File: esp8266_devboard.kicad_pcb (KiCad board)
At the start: 2 copper layers, 26.7 x 41.3 mm, 28 parts, among them P1 USB_OTG, P2 CONN_01X09, P3 CONN_01X09, SW1 MODE, SW2 RESET, U1 FT230X, U2 XC6206, U3 esp-wroom-02

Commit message: add OSHW symbol
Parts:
- added Symbol1: Symbol_OSHW-Logo_SilkScreen, Symbols:Symbol_OSHW-Logo_SilkScreen, F.Cu at (153.7, 81.7)
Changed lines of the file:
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@@
     (tracks 291)
     (zones 0)
-    (modules 28)
+    (modules 29)
     (nets 35)
   )
@@
     )
   )
+  (module Symbols:Symbol_OSHW-Logo_SilkScreen (layer F.Cu)
+    (at 153.67 81.661)
+    (descr "Symbol, OSHW-Logo, Silk Screen,")
+    (tags "Symbol, OSHW-Logo, Silk Screen,")
+    (fp_text reference Symbol1 (at 0.127 -0.127) (layer F.SilkS) hide
+      (effects (font (size 1 1) (thickness 0.15)))
+    )
+    (fp_text value Symbol_OSHW-Logo_SilkScreen (at 0.30988 6.56082) (layer F.Fab)
+      (effects (font (size 1 1) (thickness 0.15)))
+    )
+    (fp_line (start 1.66878 2.68986) (end 2.02946 4.16052) (layer F.SilkS) (width 0.15))
+    (fp_line (start 2.02946 4.16052) (end 2.30886 3.0988) (layer F.SilkS) (width 0.15))
+    (fp_line (start 2.30886 3.0988) (end 2.61874 4.17068) (layer F.SilkS) (width 0.15))
+    (fp_line (start 2.61874 4.17068) (end 2.9591 2.72034) (layer F.SilkS) (width 0.15))
+    (fp_line (start 0.24892 3.38074) (end 1.03886 3.37058) (layer F.SilkS) (width 0.15))
+    (fp_line (start 1.03886 3.37058) (end 1.04902 3.38074) (layer F.SilkS) (width 0.15))
+    (fp_line (start 1.04902 3.38074) (end 1.04902 3.37058) (layer F.SilkS) (width 0.15))
+    (fp_line (start 1.08966 2.65938) (end 1.08966 4.20116) (layer F.SilkS) (width 0.15))
+    (fp_line (start 0.20066 2.64922) (end 0.20066 4.21894) (layer F.SilkS) (width 0.15))
+    (fp_line (start 0.20066 4.21894) (end 0.21082 4.20878) (layer F.SilkS) (width 0.15))
+    (fp_line (start -0.35052 2.75082) (end -0.70104 2.66954) (layer F.SilkS) (width 0.15))
+    (fp_line (start -0.70104 2.66954) (end -1.02108 2.65938) (layer F.SilkS) (width 0.15))
+    (fp_line (start -1.02108 2.65938) (end -1.25984 2.86004) (layer F.SilkS) (width 0.15))
+    (fp_line (start -1.25984 2.86004) (end -1.29032 3.12928) (layer F.SilkS) (width 0.15))
+    (fp_line (start -1.29032 3.12928) (end -1.04902 3.37058) (layer F.SilkS) (width 0.15))
+    (fp_line (start -1.04902 3.37058) (end -0.6604 3.50012) (layer F.SilkS) (width 0.15))
+    (fp_line (start -0.6604 3.50012) (end -0.48006 3.66014) (layer F.SilkS) (width 0.15))
+    (fp_line (start -0.48006 3.66014) (end -0.43942 3.95986) (layer F.SilkS) (width 0.15))
+    (fp_line (start -0.43942 3.95986) (end -0.67056 4.18084) (layer F.SilkS) (width 0.15))
+    (fp_line (start -0.67056 4.18084) (end -0.9906 4.20878) (layer F.SilkS) (width 0.15))
+    (fp_line (start -0.9906 4.20878) (end -1.34112 4.09956) (layer F.SilkS) (width 0.15))
+    (fp_line (start -2.37998 2.64922) (end -2.6289 2.66954) (layer F.SilkS) (width 0.15))
+    (fp_line (start -2.6289 2.66954) (end -2.8702 2.91084) (layer F.SilkS) (width 0.15))
+    (fp_line (start -2.8702 2.91084) (end -2.9591 3.40106) (layer F.SilkS) (width 0.15))
+    (fp_line (start -2.9591 3.40106) (end -2.93116 3.74904) (layer F.SilkS) (width 0.15))
+    (fp_line (start -2.93116 3.74904) (end -2.7305 4.06908) (layer F.SilkS) (width 0.15))
+    (fp_line (start -2.7305 4.06908) (end -2.47904 4.191) (layer F.SilkS) (width 0.15))
+    (fp_line (start -2.47904 4.191) (end -2.16916 4.11988) (layer F.SilkS) (width 0.15))
+    (fp_line (start -2.16916 4.11988) (end -1.95072 3.93954) (layer F.SilkS) (width 0.15))
+    (fp_line (start -1.95072 3.93954) (end -1.8796 3.4798) (layer F.SilkS) (width 0.15))
+    (fp_line (start -1.8796 3.4798) (end -1.9304 3.07086) (layer F.SilkS) (width 0.15))
+    (fp_line (start -1.9304 3.07086) (end -2.03962 2.78892) (layer F.SilkS) (width 0.15))
+    (fp_line (start -2.03962 2.78892) (end -2.4003 2.65938) (layer F.SilkS) (width 0.15))
+    (fp_line (start -1.78054 0.92964) (end -2.03962 1.49098) (layer F.SilkS) (width 0.15))
+    (fp_line (start -2.03962 1.49098) (end -1.50114 2.00914) (layer F.SilkS) (width 0.15))
+    (fp_line (start -1.50114 2.00914) (end -0.98044 1.7399) (layer F.SilkS) (width 0.15))
+    (fp_line (start -0.98044 1.7399) (end -0.70104 1.89992) (layer F.SilkS) (width 0.15))
+    (fp_line (start 0.73914 1.8796) (end 1.06934 1.6891) (layer F.SilkS) (width 0.15))
+    (fp_line (start 1.06934 1.6891) (end 1.50876 2.0193) (layer F.SilkS) (width 0.15))
+    (fp_line (start 1.50876 2.0193) (end 1.9812 1.52908) (layer F.SilkS) (width 0.15))
+    (fp_line (start 1.9812 1.52908) (end 1.69926 1.04902) (layer F.SilkS) (width 0.15))
+    (fp_line (start 1.69926 1.04902) (end 1.88976 0.57912) (layer F.SilkS) (width 0.15))
+    (fp_line (start 1.88976 0.57912) (end 2.49936 0.39116) (layer F.SilkS) (width 0.15))
+    (fp_line (start 2.49936 0.39116) (end 2.49936 -0.28956) (layer F.SilkS) (width 0.15))
+    (fp_line (start 2.49936 -0.28956) (end 1.94056 -0.42926) (layer F.SilkS) (width 0.15))
+    (fp_line (start 1.94056 -0.42926) (end 1.7399 -1.00076) (layer F.SilkS) (width 0.15))
+    (fp_line (start 1.7399 -1.00076) (end 2.00914 -1.47066) (layer F.SilkS) (width 0.15))
+    (fp_line (start 2.00914 -1.47066) (end 1.53924 -1.9812) (layer F.SilkS) (width 0.15))
+    (fp_line (start 1.53924 -1.9812) (end 1.02108 -1.71958) (layer F.SilkS) (width 0.15))
+    (fp_line (start 1.02108 -1.71958) (end 0.55118 -1.92024) (layer F.SilkS) (width 0.15))
+    (fp_line (start 0.55118 -1.92024) (end 0.381 -2.46126) (layer F.SilkS) (width 0.15))
+    (fp_line (start 0.381 -2.46126) (end -0.30988 -2.47904) (layer F.SilkS) (width 0.15))
+    (fp_line (start -0.30988 -2.47904) (end -0.5207 -1.9304) (layer F.SilkS) (width 0.15))
+    (fp_line (start -0.5207 -1.9304) (end -0.9398 -1.76022) (layer F.SilkS) (width 0.15))
+    (fp_line (start -0.9398 -1.76022) (end -1.49098 -2.02946) (layer F.SilkS) (width 0.15))
+    (fp_line (start -1.49098 -2.02946) (end -2.00914 -1.50114) (layer F.SilkS) (width 0.15))
+    (fp_line (start -2.00914 -1.50114) (end -1.76022 -0.96012) (layer F.SilkS) (width 0.15))
+    (fp_line (start -1.76022 -0.96012) (end -1.9304 -0.48006) (layer F.SilkS) (width 0.15))
+    (fp_line (start -1.9304 -0.48006) (end -2.47904 -0.381) (layer F.SilkS) (width 0.15))
+    (fp_line (start -2.47904 -0.381) (end -2.4892 0.32004) (layer F.SilkS) (width 0.15))
+    (fp_line (start -2.4892 0.32004) (end -1.9304 0.5207) (layer F.SilkS) (width 0.15))
+    (fp_line (start -1.9304 0.5207) (end -1.7907 0.91948) (layer F.SilkS) (width 0.15))
+    (fp_line (start 0.35052 0.89916) (end 0.65024 0.7493) (layer F.SilkS) (width 0.15))
+    (fp_line (start 0.65024 0.7493) (end 0.8509 0.55118) (layer F.SilkS) (width 0.15))
+    (fp_line (start 0.8509 0.55118) (end 1.00076 0.14986) (layer F.SilkS) (width 0.15))
+    (fp_line (start 1.00076 0.14986) (end 1.00076 -0.24892) (layer F.SilkS) (width 0.15))
+    (fp_line (start 1.00076 -0.24892) (end 0.8509 -0.59944) (layer F.SilkS) (width 0.15))
+    (fp_line (start 0.8509 -0.59944) (end 0.39878 -0.94996) (layer F.SilkS) (width 0.15))
+    (fp_line (start 0.39878 -0.94996) (end -0.0508 -1.00076) (layer F.SilkS) (width 0.15))
+    (fp_line (start -0.0508 -1.00076) (end -0.44958 -0.89916) (layer F.SilkS) (width 0.15))
+    (fp_line (start -0.44958 -0.89916) (end -0.8509 -0.55118) (layer F.SilkS) (width 0.15))
+    (fp_line (start -0.8509 -0.55118) (end -1.00076 -0.09906) (layer F.SilkS) (width 0.15))
+    (fp_line (start -1.00076 -0.09906) (end -0.94996 0.39878) (layer F.SilkS) (width 0.15))
+    (fp_line (start -0.94996 0.39878) (end -0.70104 0.70104) (layer F.SilkS) (width 0.15))
+    (fp_line (start -0.70104 0.70104) (end -0.35052 0.89916) (layer F.SilkS) (width 0.15))
+    (fp_line (start -0.35052 0.89916) (end -0.70104 1.89992) (layer F.SilkS) (width 0.15))
+    (fp_line (start 0.35052 0.89916) (end 0.7493 1.89992) (layer F.SilkS) (width 0.15))
+  )
   (gr_text 14 (at 163.322 99.06 270) (layer F.SilkS)

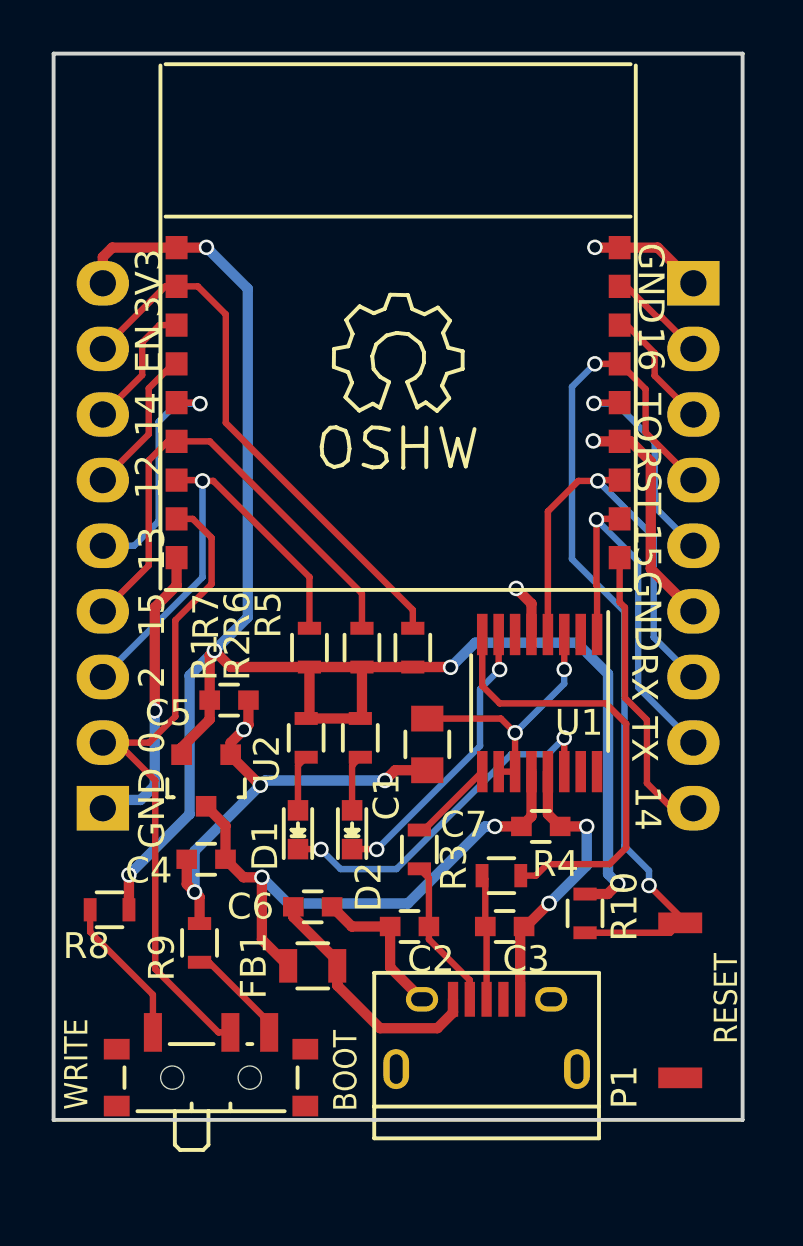
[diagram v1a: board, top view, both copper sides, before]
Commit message: commit before change FT230X to FT232R
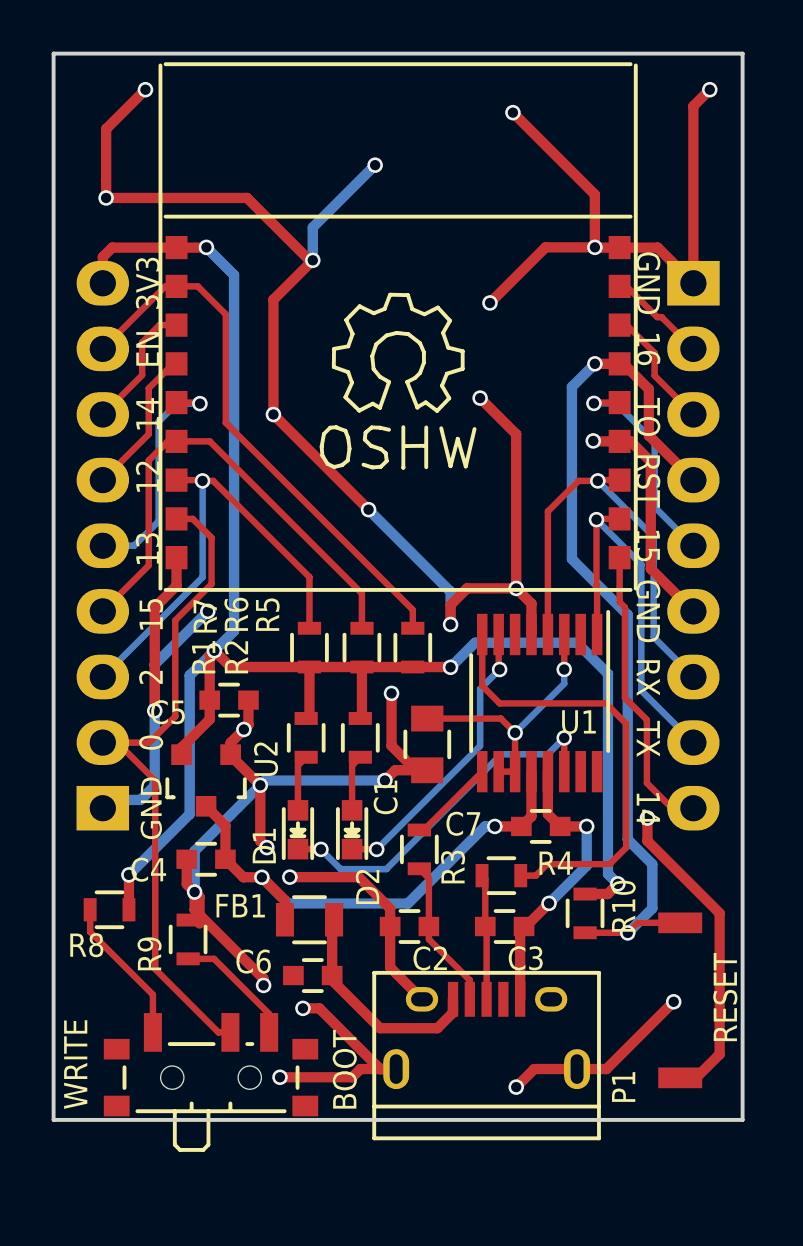
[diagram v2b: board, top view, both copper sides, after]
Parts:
- moved C6 2.66 mm to (150.4, 105.5), turned to 180 degrees
- moved FB1 1.79 mm to (150.2, 103.4)
- moved R9 0.46 mm to (145.5, 104.1)
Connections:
- net /RX renamed /RX-TX
- net /TX renamed /TX-RX
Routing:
- net GND: track 62.7 -> 176.7 mm, vias 10 -> 31
- net VDD: track 70.2 -> 67.7 mm
- net VCC: track 21.9 -> 20.1 mm
- net Net-(C6-Pad1): track 9.68 -> 8.59 mm
- net Net-(R9-Pad1): track 4.05 -> 4.74 mm

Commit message: Finish replacing FT232R
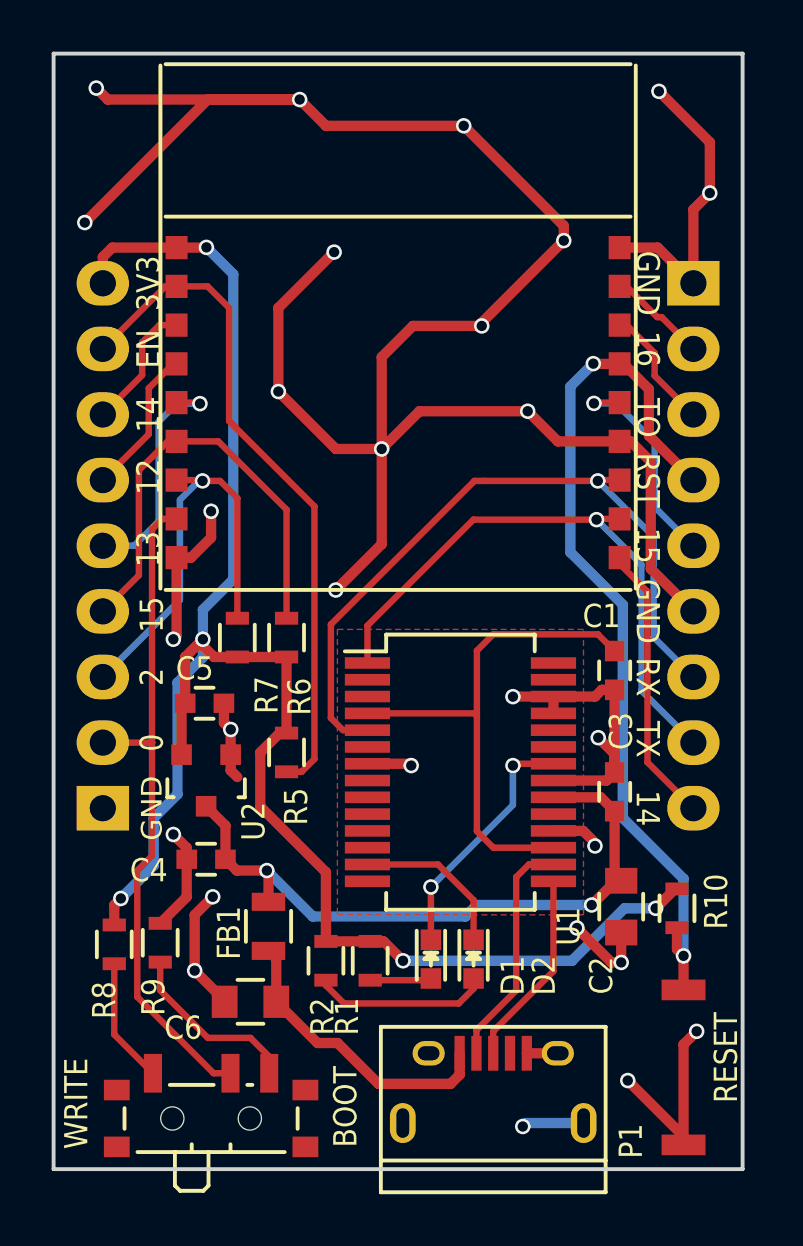
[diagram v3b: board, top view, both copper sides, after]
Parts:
- removed C7: 100nF, Capacitors_SMD:C_0603
- removed R3, R4: 27R, Resistors_SMD:R_0603
- removed Symbol1: Symbol_OSHW-Logo_SilkScreen, Symbols:Symbol_OSHW-Logo_SilkScreen
- C1: footprint Capacitors_SMD:C_0805 -> Capacitors_SMD:C_0603
- C2: value 49pF -> 4.7uF; footprint Capacitors_SMD:C_0603 -> Capacitors_SMD:C_0805
- C3: value 49pF -> 100nF
- C6: footprint Capacitors_SMD:C_0603 -> Capacitors_SMD:C_0805
- U1: value FT230X -> FT232R; footprint Housings_SSOP:QSOP-16_3.9x4.9mm_Pitch0.635mm -> Housings_SSOP:SSOP-28_5.3x10.2mm_Pitch0.65mm
- moved R1 8.98 mm to (152.6, 105.0)
- moved R2 8.73 mm to (150.9, 105.0)
- moved C2 8.23 mm to (162.3, 102.9), turned to 270 degrees
- moved C1 7.80 mm to (162.1, 93.7)
- moved D1 7.18 mm to (154.9, 104.9), turned to 270 degrees
- moved D2 6.87 mm to (156.6, 104.9), turned to 270 degrees
- moved C3 6.73 mm to (162.1, 98.4), turned to 90 degrees
- moved R5 6.35 mm to (149.4, 96.9), turned to 270 degrees
- moved U1 4.07 mm to (156.1, 97.7), turned to 0 degrees
- moved R10 3.56 mm to (164.5, 102.9)
- moved R6 2.94 mm to (149.4, 92.5)
- moved R7 2.82 mm to (147.4, 92.5)
- moved C6 2.62 mm to (148.0, 106.6)
- moved SW2 2.60 mm to (164.7, 109.1)
- moved P1 2.10 mm to (157.4, 110.1)
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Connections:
- net VDD renamed +3V3
- C2 pad 1: Net-(C2-Pad1) -> +5V
- C3 pad 1: Net-(C3-Pad1) -> +5V
- C4 pad 1: VCC -> +5V
- FB1 pad 2: VCC -> +5V
- P1 pad 2: Net-(C2-Pad1) -> /USBDM
- P1 pad 3: Net-(C3-Pad1) -> /USBDP
- P1 pad 4: Net-(P1-Pad4) -> (no net)
- U1 pad 10: Net-(C1-Pad1) -> (no net)
- U1 pad 11: Net-(C1-Pad1) -> (no net)
- U1 pad 12: VCC -> (no net)
- U1 pad 13: GND -> /CBUS2
- U1 pad 14: /CBUS1 -> (no net)
- U1 pad 15: Net-(U1-Pad15) -> /USBDP
- U1 pad 16: Net-(U1-Pad16) -> /USBDM
- U1 pad 2: Net-(U1-Pad2) -> (no net)
- U1 pad 3: Net-(C1-Pad1) -> (no net)
- U1 pad 4: /RX-TX -> Net-(C1-Pad1)
- U1 pad 5: GND -> /RX-TX
- U1 pad 6: Net-(U1-Pad6) -> (no net)
- U1 pad 7: /CBUS2 -> GND
- U1 pad 8: /USBDP -> (no net)
- U1 pad 9: /USBDM -> (no net)
- U2 pad 3: VCC -> +5V
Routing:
- net GND: track 176.7 -> 139.9 mm, vias 31 -> 28
- net +5V: track 0.00 -> 25.8 mm, vias 0 -> 2
- net VCC: track 20.1 -> 0.00 mm, vias 2 -> 0
- net /RX-TX: track 17.2 -> 27.8 mm
- net Net-(C1-Pad1): track 10.4 -> 20.4 mm, vias 2 -> 0
- net /USBDP: track 17.5 -> 7.62 mm
- net /TX-RX: track 15.5 -> 23.1 mm
- net Net-(C2-Pad1): track 5.86 -> 0.00 mm
- net /USBDM: track 3.37 -> 9.10 mm
- net /CBUS2: track 11.3 -> 6.22 mm, vias 2 -> 0
- net /EN: track 21.4 -> 26.4 mm
- net Net-(C3-Pad1): track 4.86 -> 0.00 mm
- net Net-(D2-Pad2): track 2.19 -> 6.84 mm
- net /CBUS1: track 14.0 -> 9.66 mm
- net Net-(C6-Pad1): track 8.59 -> 11.5 mm
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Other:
- board size 26.7 x 41.3 mm -> 26.7 x 43.2 mm

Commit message: modify pattern and silk
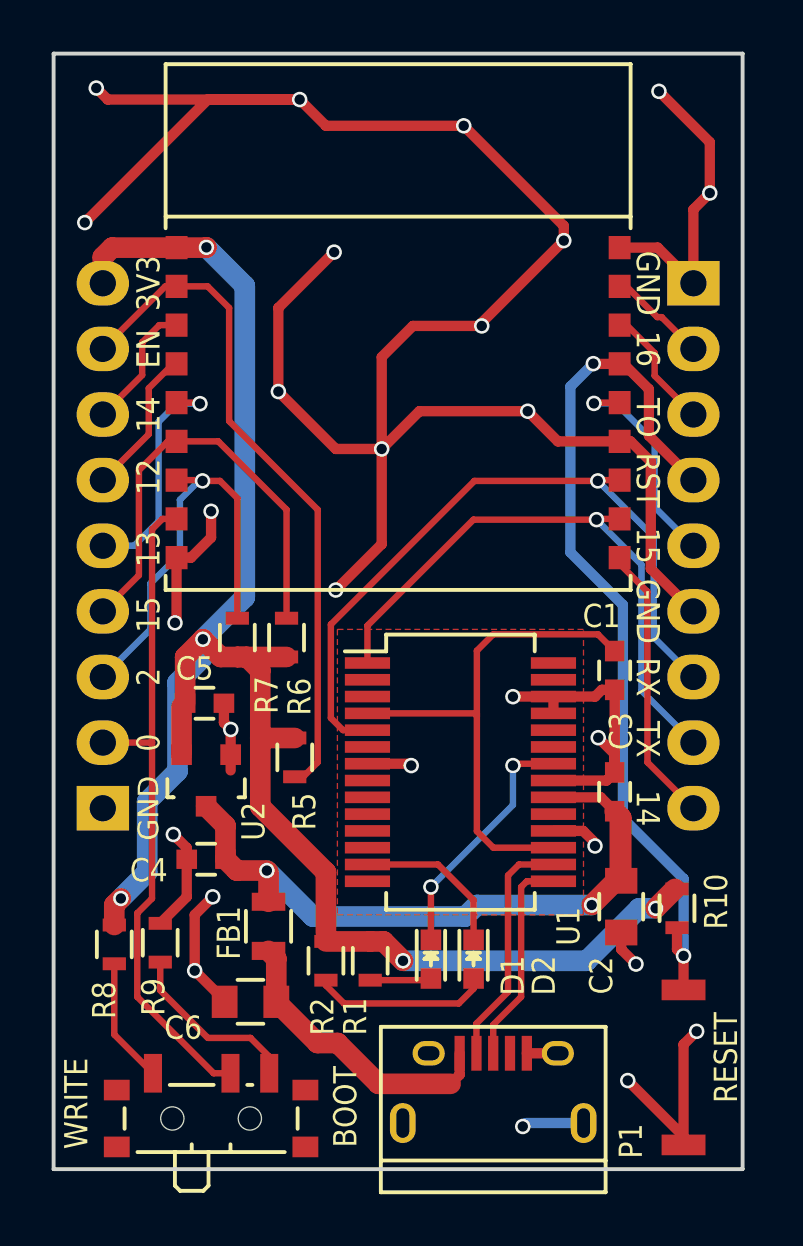
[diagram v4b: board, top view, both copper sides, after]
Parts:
- moved R5 0.37 mm to (149.7, 97.1)
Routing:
- net GND: track 139.9 -> 136.9 mm, vias 28 -> 27
- net +5V: track 25.8 -> 28.6 mm
- net +3V3: track 69.9 -> 71.5 mm
- net /USBDP: track 7.62 -> 8.23 mm
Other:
- net class PWR added: clearance 0.2, trace_width 0.8, via_dia 0.6, via_drill 0.4
